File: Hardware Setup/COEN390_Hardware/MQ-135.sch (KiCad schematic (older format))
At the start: 1 part

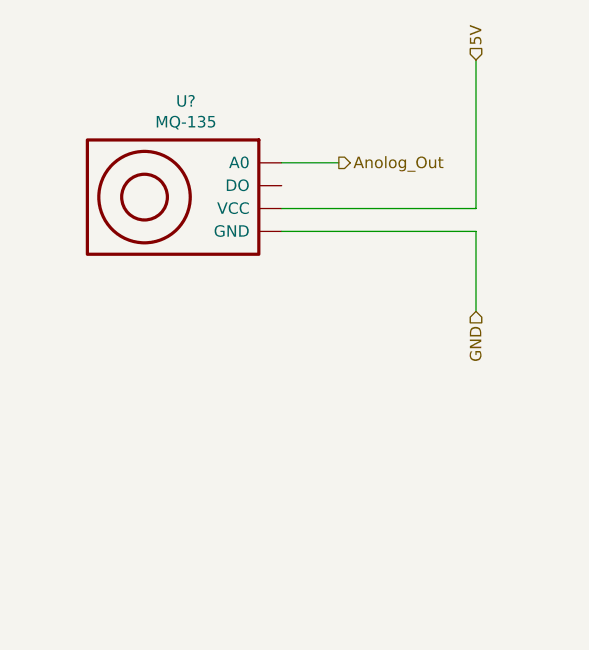
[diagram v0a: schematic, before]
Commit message: Edited Arduino set up
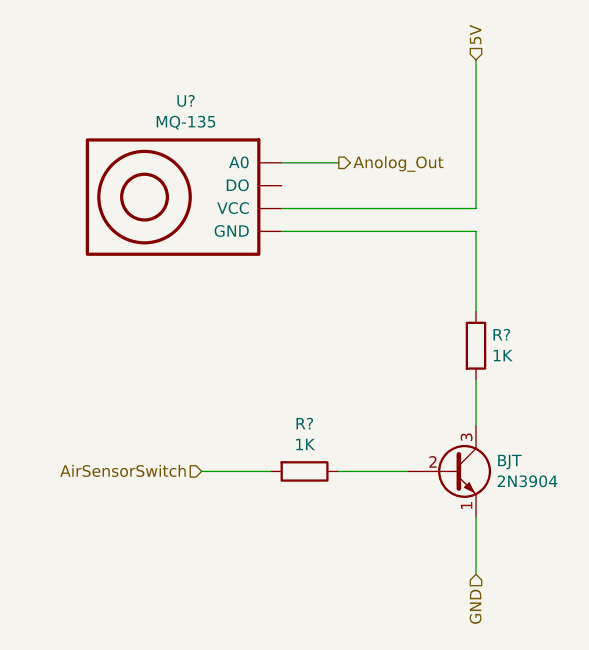
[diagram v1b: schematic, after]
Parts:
- added BJT: 2N3904, Package_TO_SOT_THT:TO-92_Inline, symbol Transistor_BJT:2N3904
- added R? (x2): 1K, symbol Device:R
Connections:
- net GND: now also BJT.1 (E); no longer U?.~ (VCC)
- new net: R?.1, U?.~ (VCC)
- new net: BJT.2 (B), R?.1
- new net: BJT.3 (C), R?.2
- new net AirSensorSwitch: R?.2
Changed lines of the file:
@@
 Text HLabel 3100 1200 1    50   Input ~ 0
 5V
-Text HLabel 3100 2300 3    50   Input ~ 0
+Text HLabel 3100 3450 3    50   Input ~ 0
 GND
 Text HLabel 2500 1650 2    50   Output ~ 0
@@
 Wire Wire Line
 	2250 1650 2500 1650
+$Comp
+L Transistor_BJT:2N3904 BJT
+U 1 1 60522CC5
+P 3000 3000
+F 0 "BJT" H 3190 3046 50  0000 L CNN
+F 1 "2N3904" H 3190 2955 50  0000 L CNN
+F 2 "Package_TO_SOT_THT:TO-92_Inline" H 3200 2925 50  0001 L CIN
+F 3 "https://www.onsemi.com/pub/Collateral/2N3903-D.PDF" H 3000 3000 50  0001 L CNN
+	1    3000 3000
+	1    0    0    -1
+$EndComp
+Wire Wire Line
+	3100 3450 3100 3200
+Text HLabel 1900 3000 0    50   Input ~ 0
+AirSensorSwitch
+$Comp
+L Device:R R?
+U 1 1 60524AFD
+P 2350 3000
+F 0 "R?" V 2143 3000 50  0000 C CNN
+F 1 "1K" V 2234 3000 50  0000 C CNN
+F 2 "" V 2280 3000 50  0001 C CNN
+F 3 "~" H 2350 3000 50  0001 C CNN
+	1    2350 3000
+	0    1    1    0
+$EndComp
+Wire Wire Line
+	2500 3000 2800 3000
+Wire Wire Line
+	2200 3000 1900 3000
+$Comp
+L Device:R R?
+U 1 1 605291CF
+P 3100 2450
+F 0 "R?" H 3170 2496 50  0000 L CNN
+F 1 "1K" H 3170 2405 50  0000 L CNN
+F 2 "" V 3030 2450 50  0001 C CNN
+F 3 "~" H 3100 2450 50  0001 C CNN
+	1    3100 2450
+	1    0    0    -1
+$EndComp
+Wire Wire Line
+	3100 2600 3100 2800
 $EndSCHEMATC
